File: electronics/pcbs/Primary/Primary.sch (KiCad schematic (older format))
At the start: 27 parts, among them J1 Line Sensor 1, J10 I2C Bus, J11 I2C Bus, J12 Battery, J13 Pololu_D24V50F5, J14 Magnet, J2 Line Sensor 2, J3 Line Sensor 3, J4 Line Sensor 4, J5 Line Sensor 5, J6 Line Sensor 6, J7 Servo, J8 Pololu_DRV8834, J9 Stepper Motor, P1 Digital, P10 CONN_01X01, P11 CONN_01X01, P12 CONN_01X01, P13 CONN_01X01, P2 Power, P3 Analog, P4 Analog, P5 PWM, P6 PWM, P7 Communication, P8 CONN_01X01, P9 CONN_01X01

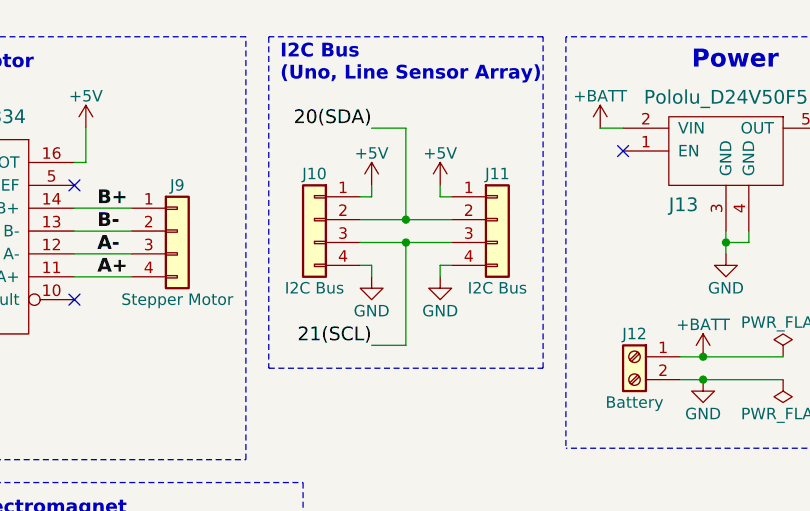
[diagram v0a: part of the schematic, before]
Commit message: Primary PCB: Removed one of the I2C bus sockets - we'll only need one.
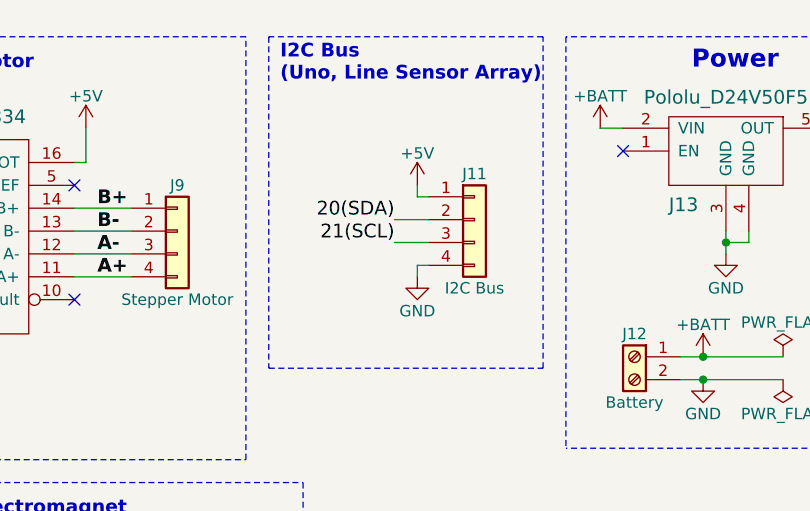
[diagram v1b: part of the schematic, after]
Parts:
- removed J10: I2C Bus, Connectors_Samtec:SL-104-X-XX_1x04, symbol Conn_01x04
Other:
- moved on the sheet: J11
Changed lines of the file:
@@
 L Conn_01x04 J11
 U 1 1 5AB0C368
-P 6600 1350
-F 0 "J11" H 6600 1550 50  0000 C CNN
-F 1 "I2C Bus" H 6600 1050 50  0000 C CNN
-F 2 "Connectors_Samtec:SL-104-X-XX_1x04" H 6600 1350 50  0001 C CNN
-F 3 "" H 6600 1350 50  0001 C CNN
-	1    6600 1350
-	1    0    0    -1
-$EndComp
-$Comp
-L Conn_01x04 J10
-U 1 1 5AB0C56B
-P 5800 1350
-F 0 "J10" H 5800 1550 50  0000 C CNN
-F 1 "I2C Bus" H 5800 1050 50  0000 C CNN
-F 2 "Connectors_Samtec:SL-104-X-XX_1x04" H 5800 1350 50  0001 C CNN
-F 3 "" H 5800 1350 50  0001 C CNN
-	1    5800 1350
-	-1   0    0    -1
+P 6500 1350
+F 0 "J11" H 6500 1550 50  0000 C CNN
+F 1 "I2C Bus" H 6500 1050 50  0000 C CNN
+F 2 "Connectors_Samtec:SL-104-X-XX_1x04" H 6500 1350 50  0001 C CNN
+F 3 "" H 6500 1350 50  0001 C CNN
+	1    6500 1350
+	1    0    0    -1
 $EndComp
 $Comp
 L +5V #PWR012
-U 1 1 5AB0C604
-P 6050 1200
-F 0 "#PWR012" H 6050 1050 50  0001 C CNN
-F 1 "+5V" H 6050 1340 50  0000 C CNN
-F 2 "" H 6050 1200 50  0000 C CNN
-F 3 "" H 6050 1200 50  0000 C CNN
-	1    6050 1200
-	1    0    0    -1
-$EndComp
-$Comp
-L +5V #PWR013
 U 1 1 5AB0C699
-P 6350 1200
-F 0 "#PWR013" H 6350 1050 50  0001 C CNN
-F 1 "+5V" H 6350 1340 50  0000 C CNN
-F 2 "" H 6350 1200 50  0000 C CNN
-F 3 "" H 6350 1200 50  0000 C CNN
-	1    6350 1200
-	1    0    0    -1
-$EndComp
-$Comp
-L GND #PWR014
-U 1 1 5AB0CA06
-P 6050 1600
-F 0 "#PWR014" H 6050 1350 50  0001 C CNN
-F 1 "GND" H 6050 1450 50  0000 C CNN
-F 2 "" H 6050 1600 50  0000 C CNN
-F 3 "" H 6050 1600 50  0000 C CNN
-	1    6050 1600
-	1    0    0    -1
-$EndComp
-$Comp
-L GND #PWR015
+P 6250 1200
+F 0 "#PWR012" H 6250 1050 50  0001 C CNN
+F 1 "+5V" H 6250 1340 50  0000 C CNN
+F 2 "" H 6250 1200 50  0000 C CNN
+F 3 "" H 6250 1200 50  0000 C CNN
+	1    6250 1200
+	1    0    0    -1
+$EndComp
+$Comp
+L GND #PWR013
 U 1 1 5AB0CA84
-P 6350 1600
-F 0 "#PWR015" H 6350 1350 50  0001 C CNN
-F 1 "GND" H 6350 1450 50  0000 C CNN
-F 2 "" H 6350 1600 50  0000 C CNN
-F 3 "" H 6350 1600 50  0000 C CNN
-	1    6350 1600
+P 6250 1600
+F 0 "#PWR013" H 6250 1350 50  0001 C CNN
+F 1 "GND" H 6250 1450 50  0000 C CNN
+F 2 "" H 6250 1600 50  0000 C CNN
+F 3 "" H 6250 1600 50  0000 C CNN
+	1    6250 1600
 	1    0    0    -1
 $EndComp
 Text Notes 5650 750  0    60   ~ 12
 I2C Bus\n(Uno, Line Sensor Array)
-Text Label 6050 950  2    60   ~ 0
+Text Label 6150 1350 2    60   ~ 0
 20(SDA)
-Text Label 6050 1900 2    60   ~ 0
+Text Label 6150 1450 2    60   ~ 0
 21(SCL)
 Wire Wire Line
@@
 	4800 1100 4750 1100
 Wire Wire Line
-	6000 1250 6050 1250
-Wire Wire Line
-	6050 1250 6050 1200
-Wire Wire Line
-	6350 1200 6350 1250
-Wire Wire Line
-	6350 1250 6400 1250
-Wire Wire Line
-	6400 1550 6350 1550
-Wire Wire Line
-	6350 1550 6350 1600
-Wire Wire Line
-	6050 1600 6050 1550
-Wire Wire Line
-	6050 1550 6000 1550
-Wire Wire Line
-	6000 1450 6400 1450
-Wire Wire Line
-	6200 1450 6200 1900
-Connection ~ 6200 1450
-Wire Wire Line
-	6000 1350 6400 1350
-Wire Wire Line
-	6200 1350 6200 950
-Connection ~ 6200 1350
+	6250 1200 6250 1250
+Wire Wire Line
+	6250 1250 6300 1250
+Wire Wire Line
+	6300 1550 6250 1550
+Wire Wire Line
+	6250 1550 6250 1600
 Wire Notes Line
 	6800 550  5600 550
@@
 Wire Notes Line
 	6800 2000 6800 550
-Wire Wire Line
-	6200 950  6050 950
-Wire Wire Line
-	6200 1900 6050 1900
 $Comp
 L Conn_01x03 J7
@@
 Servo Motor
 $Comp
-L +5V #PWR016
+L +5V #PWR014
 U 1 1 5AB127F7
 P 3550 2850
-F 0 "#PWR016" H 3550 2700 50  0001 C CNN
+F 0 "#PWR014" H 3550 2700 50  0001 C CNN
 F 1 "+5V" H 3550 2990 50  0000 C CNN
 F 2 "" H 3550 2850 50  0000 C CNN
@@
 $EndComp
 $Comp
-L GND #PWR017
+L GND #PWR015
 U 1 1 5AB1284A
 P 3550 3050
-F 0 "#PWR017" H 3550 2800 50  0001 C CNN
+F 0 "#PWR015" H 3550 2800 50  0001 C CNN
 F 1 "GND" H 3550 2900 50  0000 C CNN
 F 2 "" H 3550 3050 50  0000 C CNN
@@
 NoConn ~ 7150 1050
 $Comp
-L GND #PWR018
+L GND #PWR016
 U 1 1 5AB13861
 P 7600 1500
-F 0 "#PWR018" H 7600 1250 50  0001 C CNN
+F 0 "#PWR016" H 7600 1250 50  0001 C CNN
 F 1 "GND" H 7600 1350 50  0000 C CNN
 F 2 "" H 7600 1500 50  0000 C CNN
@@
 Connection ~ 7600 1450
 $Comp
-L +BATT #PWR019
+L +BATT #PWR017
 U 1 1 5AB13B80
 P 7050 950
-F 0 "#PWR019" H 7050 800 50  0001 C CNN
+F 0 "#PWR017" H 7050 800 50  0001 C CNN
 F 1 "+BATT" H 7050 1090 50  0000 C CNN
 F 2 "" H 7050 950 50  0001 C CNN
@@
 $EndComp
 $Comp
-L +BATT #PWR020
+L +BATT #PWR018
 U 1 1 5AB16019
 P 7500 1950
-F 0 "#PWR020" H 7500 1800 50  0001 C CNN
+F 0 "#PWR018" H 7500 1800 50  0001 C CNN
 F 1 "+BATT" H 7500 2090 50  0000 C CNN
 F 2 "" H 7500 1950 50  0001 C CNN
@@
 $EndComp
 $Comp
-L GND #PWR021
+L GND #PWR019
 U 1 1 5AB16072
 P 7500 2050
-F 0 "#PWR021" H 7500 1800 50  0001 C CNN
+F 0 "#PWR019" H 7500 1800 50  0001 C CNN
 F 1 "GND" H 7500 1900 50  0000 C CNN
 F 2 "" H 7500 2050 50  0000 C CNN
@@
 $EndComp
 $Comp
-L PWR_FLAG #FLG022
+L PWR_FLAG #FLG020
 U 1 1 5AB160ED
 P 7850 1950
-F 0 "#FLG022" H 7850 2025 50  0001 C CNN
+F 0 "#FLG020" H 7850 2025 50  0001 C CNN
 F 1 "PWR_FLAG" H 7850 2100 50  0000 C CNN
 F 2 "" H 7850 1950 50  0001 C CNN
@@
 $EndComp
 $Comp
-L PWR_FLAG #FLG023
+L PWR_FLAG #FLG021
 U 1 1 5AB1614D
 P 7850 2050
-F 0 "#FLG023" H 7850 2125 50  0001 C CNN
+F 0 "#FLG021" H 7850 2125 50  0001 C CNN
 F 1 "PWR_FLAG" H 7850 2200 50  0000 C CNN
 F 2 "" H 7850 2050 50  0001 C CNN
@@
 Connection ~ 7500 2050
 $Comp
-L PWR_FLAG #FLG024
+L PWR_FLAG #FLG022
 U 1 1 5AB1CAC7
 P 8600 850
-F 0 "#FLG024" H 8600 925 50  0001 C CNN
+F 0 "#FLG022" H 8600 925 50  0001 C CNN
 F 1 "PWR_FLAG" H 8600 1000 50  0000 C CNN
 F 2 "" H 8600 850 50  0001 C CNN
@@
 $EndComp
 $Comp
-L PWR_FLAG #FLG025
+L PWR_FLAG #FLG023
 U 1 1 5AB1CCDE
 P 9550 850
-F 0 "#FLG025" H 9550 925 50  0001 C CNN
+F 0 "#FLG023" H 9550 925 50  0001 C CNN
 F 1 "PWR_FLAG" H 9550 1000 50  0000 C CNN
 F 2 "" H 9550 850 50  0001 C CNN
@@
 $EndComp
 $Comp
-L +3.3V #PWR026
+L +3.3V #PWR024
 U 1 1 5AB1CD37
 P 9550 850
-F 0 "#PWR026" H 9550 700 50  0001 C CNN
+F 0 "#PWR024" H 9550 700 50  0001 C CNN
 F 1 "+3.3V" H 9550 990 50  0000 C CNN
 F 2 "" H 9550 850 50  0000 C CNN
@@
 $EndComp
 $Comp
-L GND #PWR027
+L GND #PWR025
 U 1 1 5AB1ECFA
 P 4650 3050
-F 0 "#PWR027" H 4650 2800 50  0001 C CNN
+F 0 "#PWR025" H 4650 2800 50  0001 C CNN
 F 1 "GND" H 4650 2900 50  0000 C CNN
 F 2 "" H 4650 3050 50  0000 C CNN
@@
 NoConn ~ 9500 4850
 $Comp
-L +5VP #PWR028
+L +5VP #PWR026
 U 1 1 5AB27247
 P 9000 1050
-F 0 "#PWR028" H 9000 900 50  0001 C CNN
+F 0 "#PWR026" H 9000 900 50  0001 C CNN
 F 1 "+5VP" H 9000 1190 50  0000 C CNN
 F 2 "" H 9000 1050 50  0001 C CNN
@@
 $EndComp
 $Comp
-L +5V #PWR029
+L +5V #PWR027
 U 1 1 5AB272C7
 P 8150 950
-F 0 "#PWR029" H 8150 800 50  0001 C CNN
+F 0 "#PWR027" H 8150 800 50  0001 C CNN
 F 1 "+5V" H 8150 1090 50  0000 C CNN
 F 2 "" H 8150 950 50  0000 C CNN
@@
 	8050 950  8150 950
 $Comp
-L +5VP #PWR030
+L +5VP #PWR028
 U 1 1 5AB2840B
 P 8600 850
-F 0 "#PWR030" H 8600 700 50  0001 C CNN
+F 0 "#PWR028" H 8600 700 50  0001 C CNN
 F 1 "+5VP" H 8600 990 50  0000 C CNN
 F 2 "" H 8600 850 50  0001 C CNN
@@
 $EndComp
 $Comp
-L GND #PWR?
+L GND #PWR029
 U 1 1 5AB165B1
 P 10600 850
-F 0 "#PWR?" H 10600 600 50  0001 C CNN
+F 0 "#PWR029" H 10600 600 50  0001 C CNN
 F 1 "GND" H 10600 700 50  0000 C CNN
 F 2 "" H 10600 850 50  0000 C CNN
@@
 Connection ~ 10900 850
 Connection ~ 11000 850
+Wire Wire Line
+	6150 1350 6300 1350
+Wire Wire Line
+	6300 1450 6150 1450
 $EndSCHEMATC

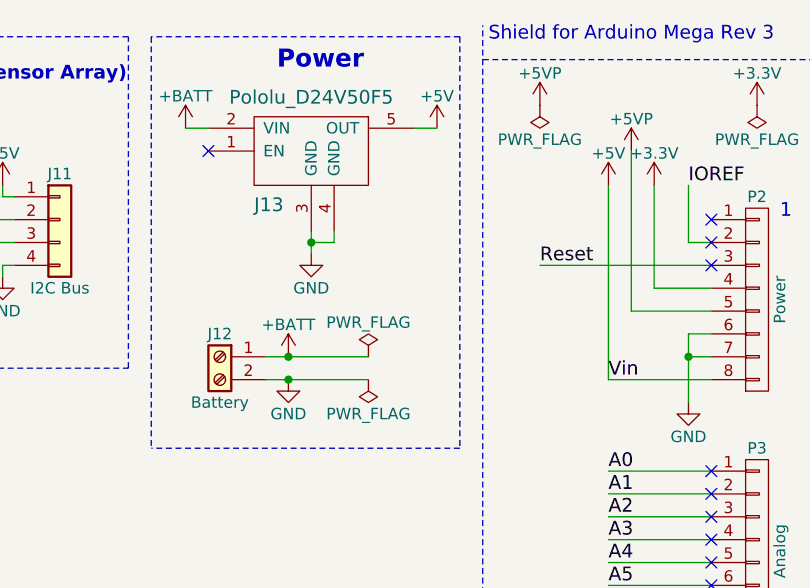
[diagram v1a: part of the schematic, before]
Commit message: Primary PCB: Power the Arduino with VBATT rather than Regulated 5V.
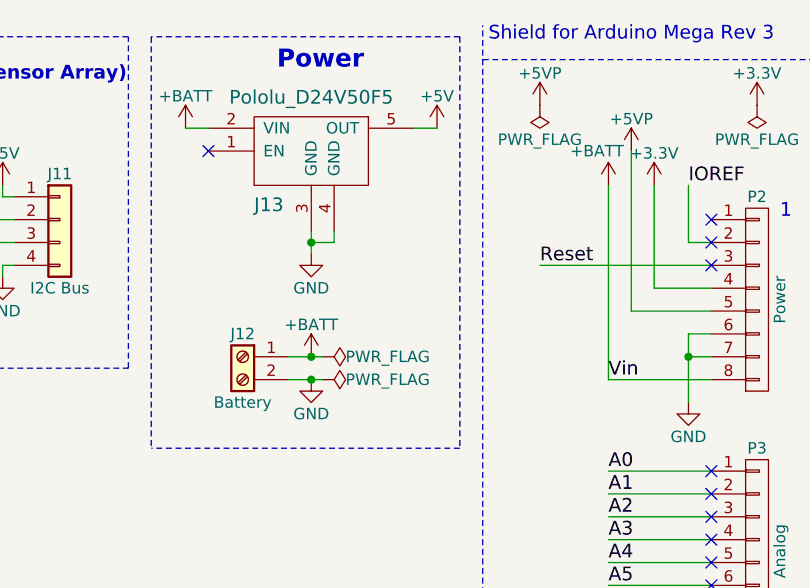
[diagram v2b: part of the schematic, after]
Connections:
- net +5V: no longer P2.8 (P8)
- net +BATT: now also P2.8 (P8)
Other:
- moved on the sheet: J12
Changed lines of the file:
@@
 Sheet 1 1
 Title "Primary Region V Bot"
-Date "mar. 31 mars 2015"
-Rev ""
+Date "2018-03-21"
+Rev "2"
 Comp "IEEE RAS (UT)"
-Comment1 ""
+Comment1 "Rev 2: The Mega is now powered by +BATT"
 Comment2 ""
 Comment3 ""
@@
 Reset
 $Comp
-L +5V #PWR02
-U 1 1 56D71D10
-P 8900 1200
-F 0 "#PWR02" H 8900 1050 50  0001 C CNN
-F 1 "+5V" H 8900 1340 50  0000 C CNN
-F 2 "" H 8900 1200 50  0000 C CNN
-F 3 "" H 8900 1200 50  0000 C CNN
-	1    8900 1200
-	1    0    0    -1
-$EndComp
-$Comp
-L GND #PWR03
+L GND #PWR02
 U 1 1 56D721E6
 P 9250 2150
-F 0 "#PWR03" H 9250 1900 50  0001 C CNN
+F 0 "#PWR02" H 9250 1900 50  0001 C CNN
 F 1 "GND" H 9250 2000 50  0000 C CNN
 F 2 "" H 9250 2150 50  0000 C CNN
@@
 $EndComp
 $Comp
-L GND #PWR04
+L GND #PWR03
 U 1 1 56D72A3D
 P 10250 2150
-F 0 "#PWR04" H 10250 1900 50  0001 C CNN
+F 0 "#PWR03" H 10250 1900 50  0001 C CNN
 F 1 "GND" H 10250 2000 50  0000 C CNN
 F 2 "" H 10250 2150 50  0000 C CNN
@@
 $EndComp
 $Comp
-L GND #PWR05
+L GND #PWR04
 U 1 1 56D758F6
 P 8650 5750
-F 0 "#PWR05" H 8650 5500 50  0001 C CNN
+F 0 "#PWR04" H 8650 5500 50  0001 C CNN
 F 1 "GND" H 8650 5600 50  0000 C CNN
 F 2 "" H 8650 5750 50  0000 C CNN
@@
 $EndComp
 $Comp
-L +5V #PWR06
+L +5V #PWR05
 U 1 1 56D75AB8
 P 10750 4550
-F 0 "#PWR06" H 10750 4400 50  0001 C CNN
+F 0 "#PWR05" H 10750 4400 50  0001 C CNN
 F 1 "+5V" H 10750 4690 50  0000 C CNN
 F 2 "" H 10750 4550 50  0000 C CNN
@@
 $EndComp
 $Comp
-L GND #PWR07
+L GND #PWR06
 U 1 1 5AB07E69
 P 2100 4150
-F 0 "#PWR07" H 2100 3900 50  0001 C CNN
+F 0 "#PWR06" H 2100 3900 50  0001 C CNN
 F 1 "GND" H 2100 4000 50  0000 C CNN
 F 2 "" H 2100 4150 50  0000 C CNN
@@
 NoConn ~ 3650 1700
 $Comp
-L GND #PWR08
+L GND #PWR07
 U 1 1 5AB0A94E
 P 4150 2150
-F 0 "#PWR08" H 4150 1900 50  0001 C CNN
+F 0 "#PWR07" H 4150 1900 50  0001 C CNN
 F 1 "GND" H 4150 2000 50  0000 C CNN
 F 2 "" H 4150 2150 50  0000 C CNN
@@
 Stepper Motor
 $Comp
-L +5V #PWR09
+L +5V #PWR08
 U 1 1 5AB0B79A
 P 2000 1000
-F 0 "#PWR09" H 2000 850 50  0001 C CNN
+F 0 "#PWR08" H 2000 850 50  0001 C CNN
 F 1 "+5V" H 2000 1140 50  0000 C CNN
 F 2 "" H 2000 1000 50  0000 C CNN
@@
 $EndComp
 $Comp
-L +5V #PWR010
+L +5V #PWR09
 U 1 1 5AB0BB75
 P 3550 950
-F 0 "#PWR010" H 3550 800 50  0001 C CNN
+F 0 "#PWR09" H 3550 800 50  0001 C CNN
 F 1 "+5V" H 3550 1090 50  0000 C CNN
 F 2 "" H 3550 950 50  0000 C CNN
@@
 $EndComp
 $Comp
-L +5V #PWR011
+L +5V #PWR010
 U 1 1 5AB0BCF7
 P 4800 950
-F 0 "#PWR011" H 4800 800 50  0001 C CNN
+F 0 "#PWR010" H 4800 800 50  0001 C CNN
 F 1 "+5V" H 4800 1090 50  0000 C CNN
 F 2 "" H 4800 950 50  0000 C CNN
@@
 $EndComp
 $Comp
-L +5V #PWR012
+L +5V #PWR011
 U 1 1 5AB0C699
 P 6250 1200
-F 0 "#PWR012" H 6250 1050 50  0001 C CNN
+F 0 "#PWR011" H 6250 1050 50  0001 C CNN
 F 1 "+5V" H 6250 1340 50  0000 C CNN
 F 2 "" H 6250 1200 50  0000 C CNN
@@
 $EndComp
 $Comp
-L GND #PWR013
+L GND #PWR012
 U 1 1 5AB0CA84
 P 6250 1600
-F 0 "#PWR013" H 6250 1350 50  0001 C CNN
+F 0 "#PWR012" H 6250 1350 50  0001 C CNN
 F 1 "GND" H 6250 1450 50  0000 C CNN
 F 2 "" H 6250 1600 50  0000 C CNN
@@
 Servo Motor
 $Comp
-L +5V #PWR014
+L +5V #PWR013
 U 1 1 5AB127F7
 P 3550 2850
-F 0 "#PWR014" H 3550 2700 50  0001 C CNN
+F 0 "#PWR013" H 3550 2700 50  0001 C CNN
 F 1 "+5V" H 3550 2990 50  0000 C CNN
 F 2 "" H 3550 2850 50  0000 C CNN
@@
 $EndComp
 $Comp
-L GND #PWR015
+L GND #PWR014
 U 1 1 5AB1284A
 P 3550 3050
-F 0 "#PWR015" H 3550 2800 50  0001 C CNN
+F 0 "#PWR014" H 3550 2800 50  0001 C CNN
 F 1 "GND" H 3550 2900 50  0000 C CNN
 F 2 "" H 3550 3050 50  0000 C CNN
@@
 NoConn ~ 7150 1050
 $Comp
-L GND #PWR016
+L GND #PWR015
 U 1 1 5AB13861
 P 7600 1500
-F 0 "#PWR016" H 7600 1250 50  0001 C CNN
+F 0 "#PWR015" H 7600 1250 50  0001 C CNN
 F 1 "GND" H 7600 1350 50  0000 C CNN
 F 2 "" H 7600 1500 50  0000 C CNN
@@
 Connection ~ 7600 1450
 $Comp
-L +BATT #PWR017
+L +BATT #PWR016
 U 1 1 5AB13B80
 P 7050 950
-F 0 "#PWR017" H 7050 800 50  0001 C CNN
+F 0 "#PWR016" H 7050 800 50  0001 C CNN
 F 1 "+BATT" H 7050 1090 50  0000 C CNN
 F 2 "" H 7050 950 50  0001 C CNN
@@
 L Screw_Terminal_01x02 J12
 U 1 1 5AB15F1B
-P 7200 1950
-F 0 "J12" H 7200 2050 50  0000 C CNN
-F 1 "Battery" H 7200 1750 50  0000 C CNN
-F 2 "Connectors_Terminal_Blocks:TerminalBlock_bornier-2_P5.08mm" H 7200 1950 50  0001 C CNN
-F 3 "" H 7200 1950 50  0001 C CNN
-	1    7200 1950
+P 7300 1950
+F 0 "J12" H 7300 2050 50  0000 C CNN
+F 1 "Battery" H 7300 1750 50  0000 C CNN
+F 2 "Connectors_Terminal_Blocks:TerminalBlock_bornier-2_P5.08mm" H 7300 1950 50  0001 C CNN
+F 3 "" H 7300 1950 50  0001 C CNN
+	1    7300 1950
 	-1   0    0    -1
 $EndComp
 $Comp
-L +BATT #PWR018
+L +BATT #PWR017
 U 1 1 5AB16019
-P 7500 1950
-F 0 "#PWR018" H 7500 1800 50  0001 C CNN
-F 1 "+BATT" H 7500 2090 50  0000 C CNN
-F 2 "" H 7500 1950 50  0001 C CNN
-F 3 "" H 7500 1950 50  0001 C CNN
-	1    7500 1950
-	1    0    0    -1
-$EndComp
-$Comp
-L GND #PWR019
+P 7600 1950
+F 0 "#PWR017" H 7600 1800 50  0001 C CNN
+F 1 "+BATT" H 7600 2090 50  0000 C CNN
+F 2 "" H 7600 1950 50  0001 C CNN
+F 3 "" H 7600 1950 50  0001 C CNN
+	1    7600 1950
+	1    0    0    -1
+$EndComp
+$Comp
+L GND #PWR018
 U 1 1 5AB16072
-P 7500 2050
-F 0 "#PWR019" H 7500 1800 50  0001 C CNN
-F 1 "GND" H 7500 1900 50  0000 C CNN
-F 2 "" H 7500 2050 50  0000 C CNN
-F 3 "" H 7500 2050 50  0000 C CNN
-	1    7500 2050
-	1    0    0    -1
+P 7600 2050
+F 0 "#PWR018" H 7600 1800 50  0001 C CNN
+F 1 "GND" H 7600 1900 50  0000 C CNN
+F 2 "" H 7600 2050 50  0000 C CNN
+F 3 "" H 7600 2050 50  0000 C CNN
+	1    7600 2050
+	1    0    0    -1
+$EndComp
+$Comp
+L PWR_FLAG #FLG019
+U 1 1 5AB160ED
+P 7650 1950
+F 0 "#FLG019" H 7650 2025 50  0001 C CNN
+F 1 "PWR_FLAG" V 7650 2050 50  0000 L CNN
+F 2 "" H 7650 1950 50  0001 C CNN
+F 3 "" H 7650 1950 50  0001 C CNN
+	1    7650 1950
+	0    1    1    0
 $EndComp
 $Comp
 L PWR_FLAG #FLG020
-U 1 1 5AB160ED
-P 7850 1950
-F 0 "#FLG020" H 7850 2025 50  0001 C CNN
-F 1 "PWR_FLAG" H 7850 2100 50  0000 C CNN
-F 2 "" H 7850 1950 50  0001 C CNN
-F 3 "" H 7850 1950 50  0001 C CNN
-	1    7850 1950
-	1    0    0    -1
-$EndComp
-$Comp
-L PWR_FLAG #FLG021
 U 1 1 5AB1614D
-P 7850 2050
-F 0 "#FLG021" H 7850 2125 50  0001 C CNN
-F 1 "PWR_FLAG" H 7850 2200 50  0000 C CNN
-F 2 "" H 7850 2050 50  0001 C CNN
-F 3 "" H 7850 2050 50  0001 C CNN
-	1    7850 2050
-	1    0    0    1
+P 7650 2050
+F 0 "#FLG020" H 7650 2125 50  0001 C CNN
+F 1 "PWR_FLAG" V 7650 2150 50  0000 L CNN
+F 2 "" H 7650 2050 50  0001 C CNN
+F 3 "" H 7650 2050 50  0001 C CNN
+	1    7650 2050
+	0    1    -1   0
 $EndComp
 NoConn ~ 10150 1150
@@
 NoConn ~ 9000 5350
 Wire Wire Line
-	7400 1950 7850 1950
-Connection ~ 7500 1950
-Wire Wire Line
-	7400 2050 7850 2050
-Connection ~ 7500 2050
-$Comp
-L PWR_FLAG #FLG022
+	7500 1950 7650 1950
+Connection ~ 7600 1950
+Wire Wire Line
+	7500 2050 7650 2050
+Connection ~ 7600 2050
+$Comp
+L PWR_FLAG #FLG021
 U 1 1 5AB1CAC7
 P 8600 850
-F 0 "#FLG022" H 8600 925 50  0001 C CNN
+F 0 "#FLG021" H 8600 925 50  0001 C CNN
 F 1 "PWR_FLAG" H 8600 1000 50  0000 C CNN
 F 2 "" H 8600 850 50  0001 C CNN
@@
 $EndComp
 $Comp
-L PWR_FLAG #FLG023
+L PWR_FLAG #FLG022
 U 1 1 5AB1CCDE
 P 9550 850
-F 0 "#FLG023" H 9550 925 50  0001 C CNN
+F 0 "#FLG022" H 9550 925 50  0001 C CNN
 F 1 "PWR_FLAG" H 9550 1000 50  0000 C CNN
 F 2 "" H 9550 850 50  0001 C CNN
@@
 $EndComp
 $Comp
-L +3.3V #PWR024
+L +3.3V #PWR023
 U 1 1 5AB1CD37
 P 9550 850
-F 0 "#PWR024" H 9550 700 50  0001 C CNN
+F 0 "#PWR023" H 9550 700 50  0001 C CNN
 F 1 "+3.3V" H 9550 990 50  0000 C CNN
 F 2 "" H 9550 850 50  0000 C CNN
@@
 $EndComp
 $Comp
-L GND #PWR025
+L GND #PWR024
 U 1 1 5AB1ECFA
 P 4650 3050
-F 0 "#PWR025" H 4650 2800 50  0001 C CNN
+F 0 "#PWR024" H 4650 2800 50  0001 C CNN
 F 1 "GND" H 4650 2900 50  0000 C CNN
 F 2 "" H 4650 3050 50  0000 C CNN
@@
 NoConn ~ 9500 4850
 $Comp
-L +5VP #PWR026
+L +5VP #PWR025
 U 1 1 5AB27247
 P 9000 1050
-F 0 "#PWR026" H 9000 900 50  0001 C CNN
+F 0 "#PWR025" H 9000 900 50  0001 C CNN
 F 1 "+5VP" H 9000 1190 50  0000 C CNN
 F 2 "" H 9000 1050 50  0001 C CNN
@@
 $EndComp
 $Comp
-L +5V #PWR027
+L +5V #PWR026
 U 1 1 5AB272C7
 P 8150 950
-F 0 "#PWR027" H 8150 800 50  0001 C CNN
+F 0 "#PWR026" H 8150 800 50  0001 C CNN
 F 1 "+5V" H 8150 1090 50  0000 C CNN
 F 2 "" H 8150 950 50  0000 C CNN
@@
 	8050 950  8150 950
 $Comp
-L +5VP #PWR028
+L +5VP #PWR027
 U 1 1 5AB2840B
 P 8600 850
-F 0 "#PWR028" H 8600 700 50  0001 C CNN
+F 0 "#PWR027" H 8600 700 50  0001 C CNN
 F 1 "+5VP" H 8600 990 50  0000 C CNN
 F 2 "" H 8600 850 50  0001 C CNN
@@
 $EndComp
 $Comp
-L GND #PWR029
+L GND #PWR028
 U 1 1 5AB165B1
 P 10600 850
-F 0 "#PWR029" H 10600 600 50  0001 C CNN
+F 0 "#PWR028" H 10600 600 50  0001 C CNN
 F 1 "GND" H 10600 700 50  0000 C CNN
 F 2 "" H 10600 850 50  0000 C CNN
@@
 Wire Wire Line
 	6300 1450 6150 1450
+$Comp
+L +BATT #PWR029
+U 1 1 5AB2CF23
+P 8900 1200
+F 0 "#PWR029" H 8900 1050 50  0001 C CNN
+F 1 "+BATT" H 8850 1350 50  0000 C CNN
+F 2 "" H 8900 1200 50  0001 C CNN
+F 3 "" H 8900 1200 50  0001 C CNN
+	1    8900 1200
+	1    0    0    -1
+$EndComp
 $EndSCHEMATC
